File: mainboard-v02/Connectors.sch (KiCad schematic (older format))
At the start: 13 parts, among them J1 503182-1852, J2 Conn_01x05, J3 10118194-0001LF, J4 DCJ0303, U8 MR25H40MDF

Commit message: fixing bold font and adding schematic pdf of v02
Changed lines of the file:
@@
 EESchema Schematic File Version 4
-LIBS:mainboard
 EELAYER 29 0
 EELAYER END
@@
 Wire Wire Line
 	7900 5200 7900 5300
-Text GLabel 7900 5200 0    10   BiDi ~ 0
+Text GLabel 7900 5200 0    10   BiDi ~ 2
 GND
 Wire Wire Line
 	7000 3700 7000 3500
-Text GLabel 7000 3700 0    10   BiDi ~ 0
+Text GLabel 7000 3700 0    10   BiDi ~ 2
 GND
 Wire Wire Line
 	6400 3300 6400 3400
-Text GLabel 6400 3300 0    10   BiDi ~ 0
+Text GLabel 6400 3300 0    10   BiDi ~ 2
 GND
 Wire Wire Line
@@
 Wire Wire Line
 	3000 2400 3000 2500
-Text GLabel 2900 2400 0    10   BiDi ~ 0
+Text GLabel 2900 2400 0    10   BiDi ~ 2
 GND
 Wire Wire Line
@@
 Wire Wire Line
 	3600 1700 3600 2500
-Text GLabel 2900 1700 0    10   BiDi ~ 0
+Text GLabel 2900 1700 0    10   BiDi ~ 2
 GND
 Wire Wire Line
 	2300 4700 2300 4800
-Text GLabel 2300 4700 0    10   BiDi ~ 0
+Text GLabel 2300 4700 0    10   BiDi ~ 2
 GND
 Wire Wire Line
 	3500 4800 3500 4900
-Text GLabel 3500 4800 0    10   BiDi ~ 0
+Text GLabel 3500 4800 0    10   BiDi ~ 2
 GND
 Wire Wire Line
@@
 Wire Wire Line
 	3600 1500 3600 1300
-Text GLabel 2900 1500 0    10   BiDi ~ 0
+Text GLabel 2900 1500 0    10   BiDi ~ 2
 3.3V
 Wire Wire Line
@@
 Wire Wire Line
 	3600 4400 3600 4100
-Text GLabel 3500 4400 0    10   BiDi ~ 0
+Text GLabel 3500 4400 0    10   BiDi ~ 2
 3.3V
 Text GLabel 2550 6650 0    50   BiDi ~ 0
@@
 Text Notes 7200 5300 0    59   ~ 0
 Rail Switch\nConnection
-Text Notes 2600 6100 0    85   ~ 0
+Text Notes 2600 6100 0    85   ~ 17
 JTAG
-Text Notes 6400 2500 0    85   ~ 0
+Text Notes 6400 2500 0    85   ~ 17
 Power Connectors: USB, Barrel Plug, Battery
-Text Notes 2400 900  0    85   ~ 0
+Text Notes 2400 900  0    85   ~ 17
 MicroSD Card
-Text Notes 1900 3400 0    100  ~ 0
+Text Notes 1900 3400 0    100  ~ 20
 MRAM - Nonvolatile Memory\n     (4MB storage)
 $Comp
@@
 Wire Wire Line
 	2550 6450 2750 6450
-Text GLabel 2550 6850 0    10   BiDi ~ 0
+Text GLabel 2550 6850 0    10   BiDi ~ 2
 GND
 $Comp
@@
 	1    0    0    -1
 $EndComp
-Text GLabel 2550 6750 0    46   Input ~ 0
+Text GLabel 2550 6750 0    46   Input ~ 9
 ~RESET
 Wire Wire Line
@@
 	1    0    0    -1
 $EndComp
-Text GLabel 3850 4400 2    10   BiDi ~ 0
-GND
-$Comp
+Text GLabel 3850 4400 2    10   BiDi ~ 2
+GND
+$Comp

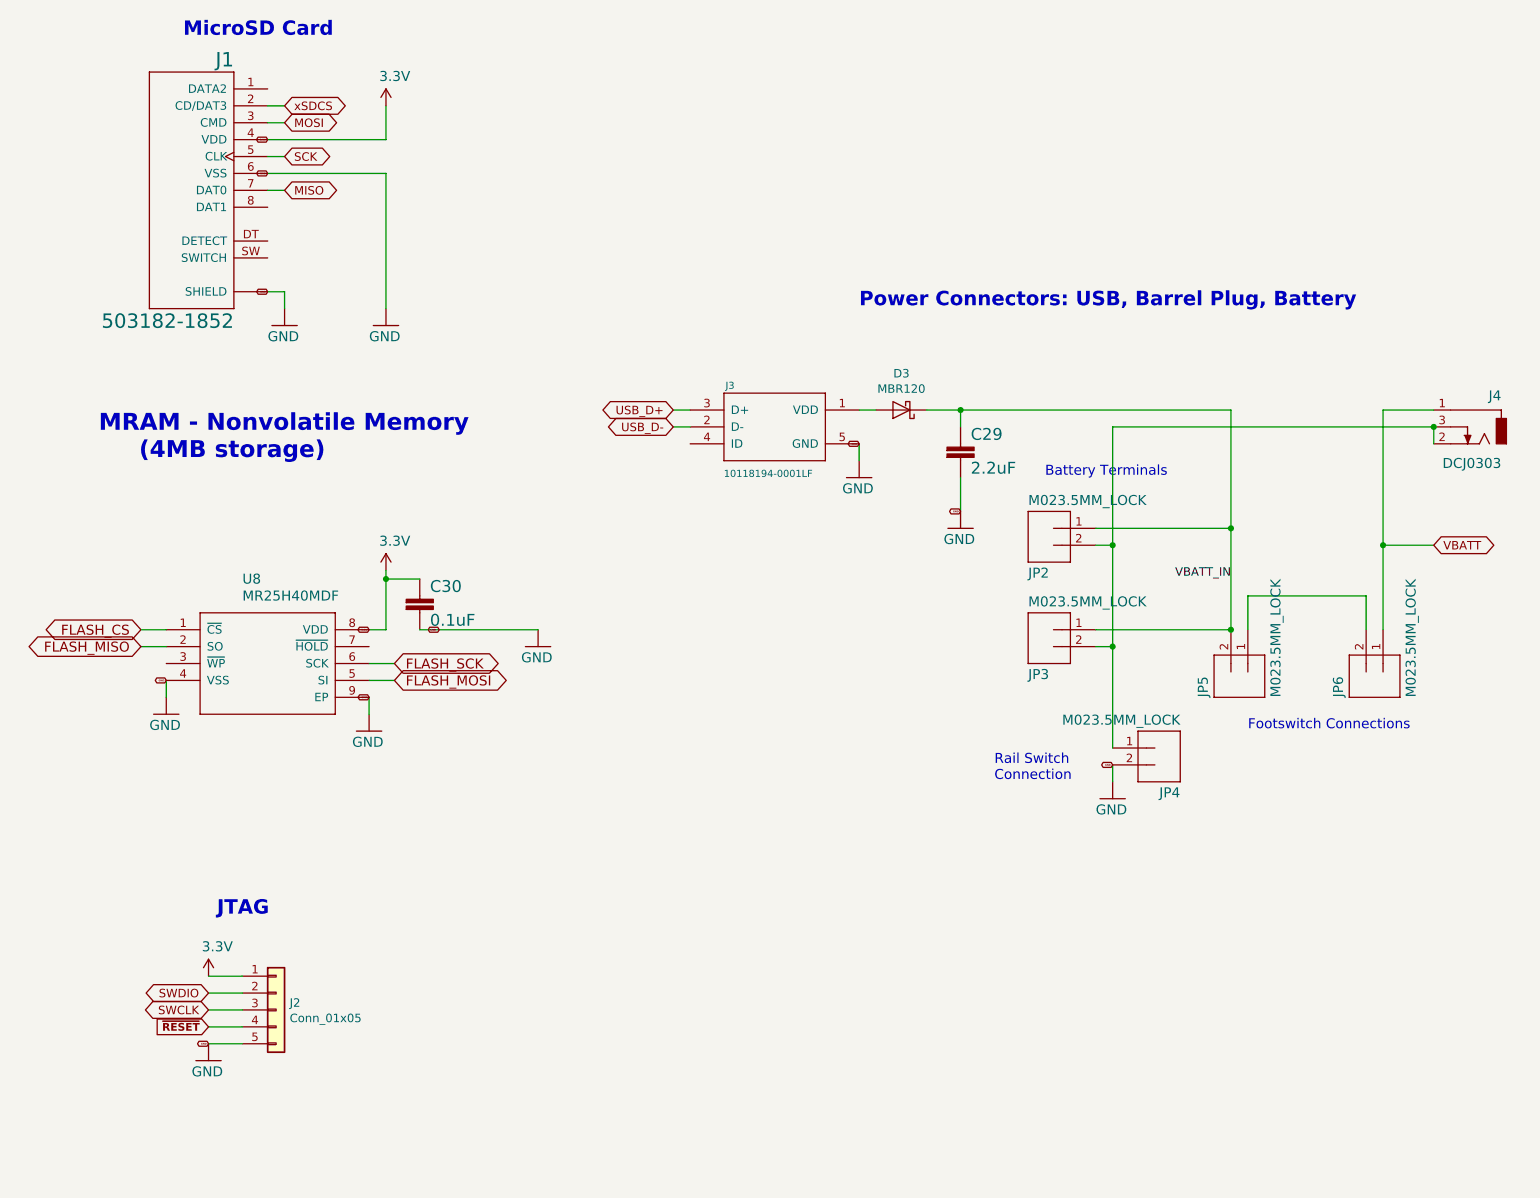
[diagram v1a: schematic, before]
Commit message: mainboard-v02 with RFM98PW
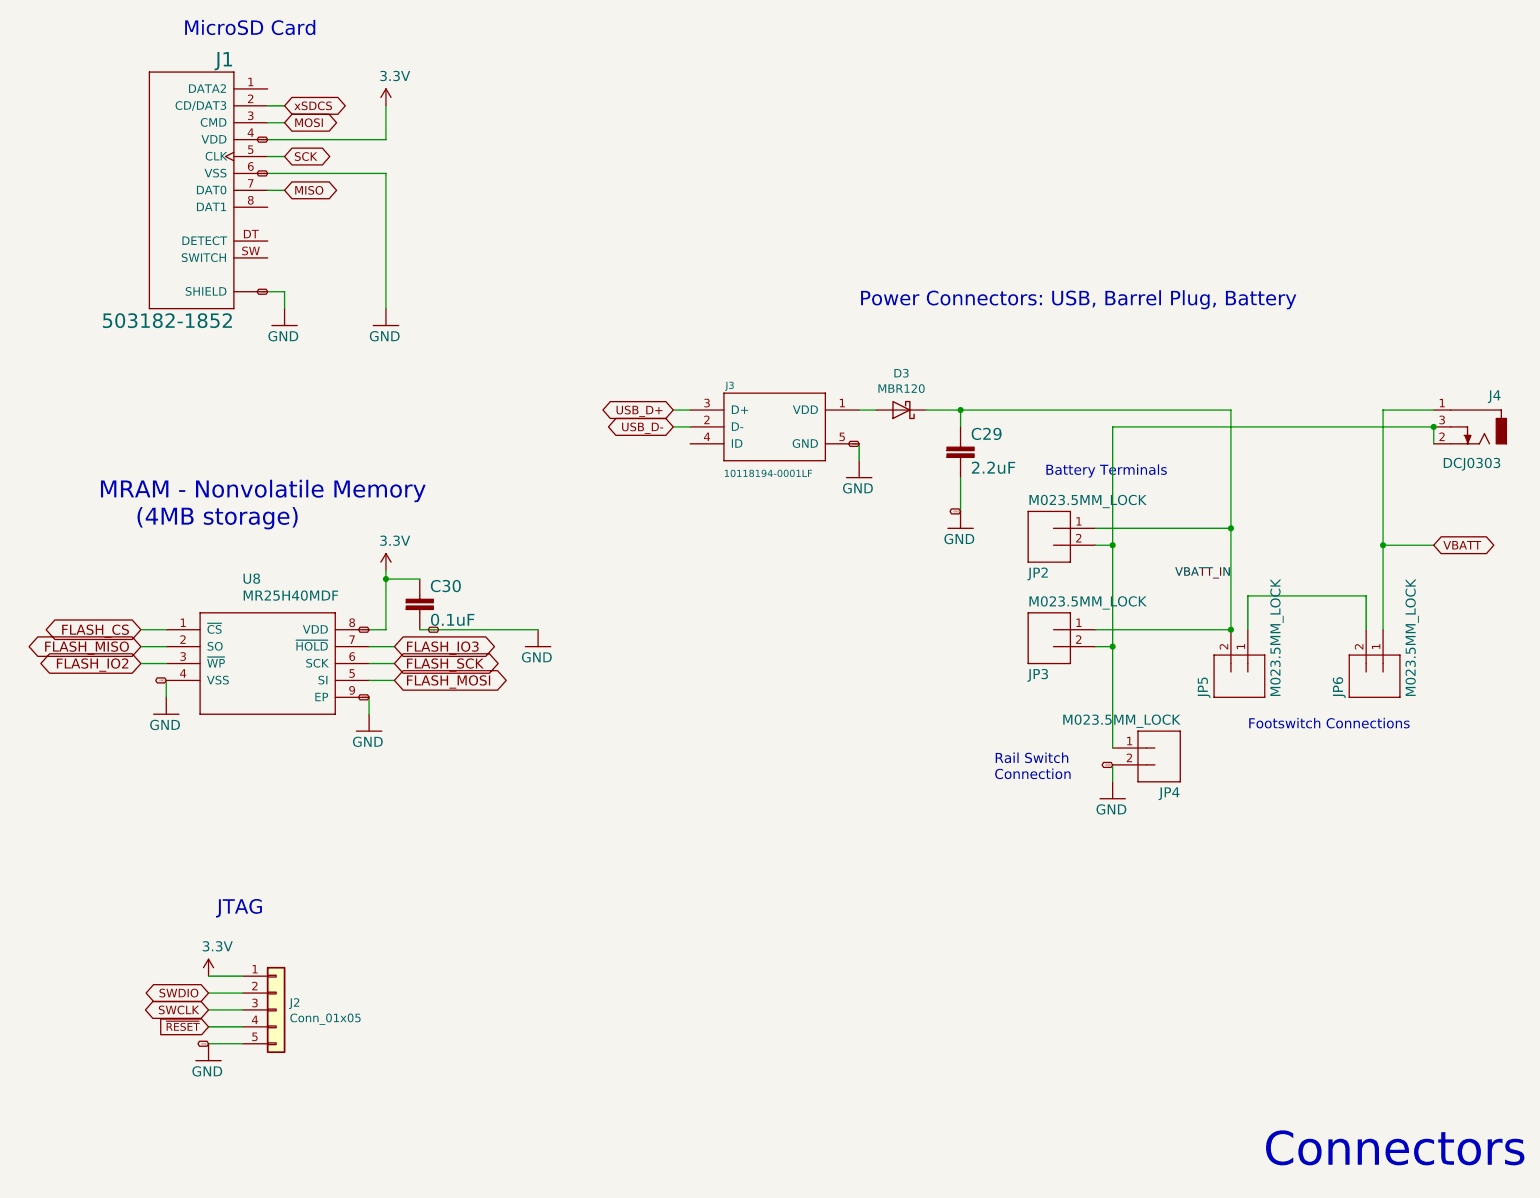
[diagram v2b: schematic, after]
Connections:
- net FLASH_IO2: now reaches U8.3 (~WP)
- net FLASH_IO3: now reaches U8.7 (~HOLD)
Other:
- note added: "Connectors"
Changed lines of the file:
@@
 EESchema Schematic File Version 4
+LIBS:mainboard-cache
 EELAYER 29 0
 EELAYER END
@@
 Wire Wire Line
 	7900 5200 7900 5300
-Text GLabel 7900 5200 0    10   BiDi ~ 2
+Text GLabel 7900 5200 0    10   BiDi ~ 0
 GND
 Wire Wire Line
 	7000 3700 7000 3500
-Text GLabel 7000 3700 0    10   BiDi ~ 2
+Text GLabel 7000 3700 0    10   BiDi ~ 0
 GND
 Wire Wire Line
 	6400 3300 6400 3400
-Text GLabel 6400 3300 0    10   BiDi ~ 2
+Text GLabel 6400 3300 0    10   BiDi ~ 0
 GND
 Wire Wire Line
@@
 Wire Wire Line
 	3000 2400 3000 2500
-Text GLabel 2900 2400 0    10   BiDi ~ 2
+Text GLabel 2900 2400 0    10   BiDi ~ 0
 GND
 Wire Wire Line
@@
 Wire Wire Line
 	3600 1700 3600 2500
-Text GLabel 2900 1700 0    10   BiDi ~ 2
+Text GLabel 2900 1700 0    10   BiDi ~ 0
 GND
 Wire Wire Line
 	2300 4700 2300 4800
-Text GLabel 2300 4700 0    10   BiDi ~ 2
+Text GLabel 2300 4700 0    10   BiDi ~ 0
 GND
 Wire Wire Line
 	3500 4800 3500 4900
-Text GLabel 3500 4800 0    10   BiDi ~ 2
+Text GLabel 3500 4800 0    10   BiDi ~ 0
 GND
 Wire Wire Line
@@
 Wire Wire Line
 	3600 1500 3600 1300
-Text GLabel 2900 1500 0    10   BiDi ~ 2
+Text GLabel 2900 1500 0    10   BiDi ~ 0
 3.3V
 Wire Wire Line
@@
 Wire Wire Line
 	3600 4400 3600 4100
-Text GLabel 3500 4400 0    10   BiDi ~ 2
+Text GLabel 3500 4400 0    10   BiDi ~ 0
 3.3V
 Text GLabel 2550 6650 0    50   BiDi ~ 0
@@
 Text Notes 7200 5300 0    59   ~ 0
 Rail Switch\nConnection
-Text Notes 2600 6100 0    85   ~ 17
+Text Notes 2600 6100 0    85   ~ 0
 JTAG
-Text Notes 6400 2500 0    85   ~ 17
+Text Notes 6400 2500 0    85   ~ 0
 Power Connectors: USB, Barrel Plug, Battery
-Text Notes 2400 900  0    85   ~ 17
+Text Notes 2400 900  0    85   ~ 0
 MicroSD Card
-Text Notes 1900 3400 0    100  ~ 20
+Text Notes 1900 3800 0    100  ~ 0
 MRAM - Nonvolatile Memory\n     (4MB storage)
 $Comp
@@
 Wire Wire Line
 	2550 6450 2750 6450
-Text GLabel 2550 6850 0    10   BiDi ~ 2
+Text GLabel 2550 6850 0    10   BiDi ~ 0
 GND
 $Comp
@@
 	1    0    0    -1
 $EndComp
-Text GLabel 2550 6750 0    46   Input ~ 9
+Text GLabel 2550 6750 0    46   Input ~ 0
 ~RESET
 Wire Wire Line
@@
 	1    0    0    -1
 $EndComp
-Text GLabel 3850 4400 2    10   BiDi ~ 2
+Text GLabel 3850 4400 2    10   BiDi ~ 0
 GND
 $Comp
@@
 	1    0    0    -1
 $EndComp
+Text GLabel 3650 4500 2    59   BiDi ~ 0
+FLASH_IO3
+Wire Wire Line
+	3650 4500 3500 4500
+Text GLabel 2150 4600 0    59   BiDi ~ 0
+FLASH_IO2
+Wire Wire Line
+	2150 4600 2300 4600
+Text Notes 10350 7600 2    200  ~ 0
+Connectors
 $EndSCHEMATC
